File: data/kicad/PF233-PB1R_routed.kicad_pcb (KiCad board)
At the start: 4 copper layers, 70 x 70 mm, 39 parts, among them M12 12 V 1.5 A switching module, Q1A 650V SJ 95mR, Q1B 650V SJ 95mR, U1 TC4420, U3 LM393

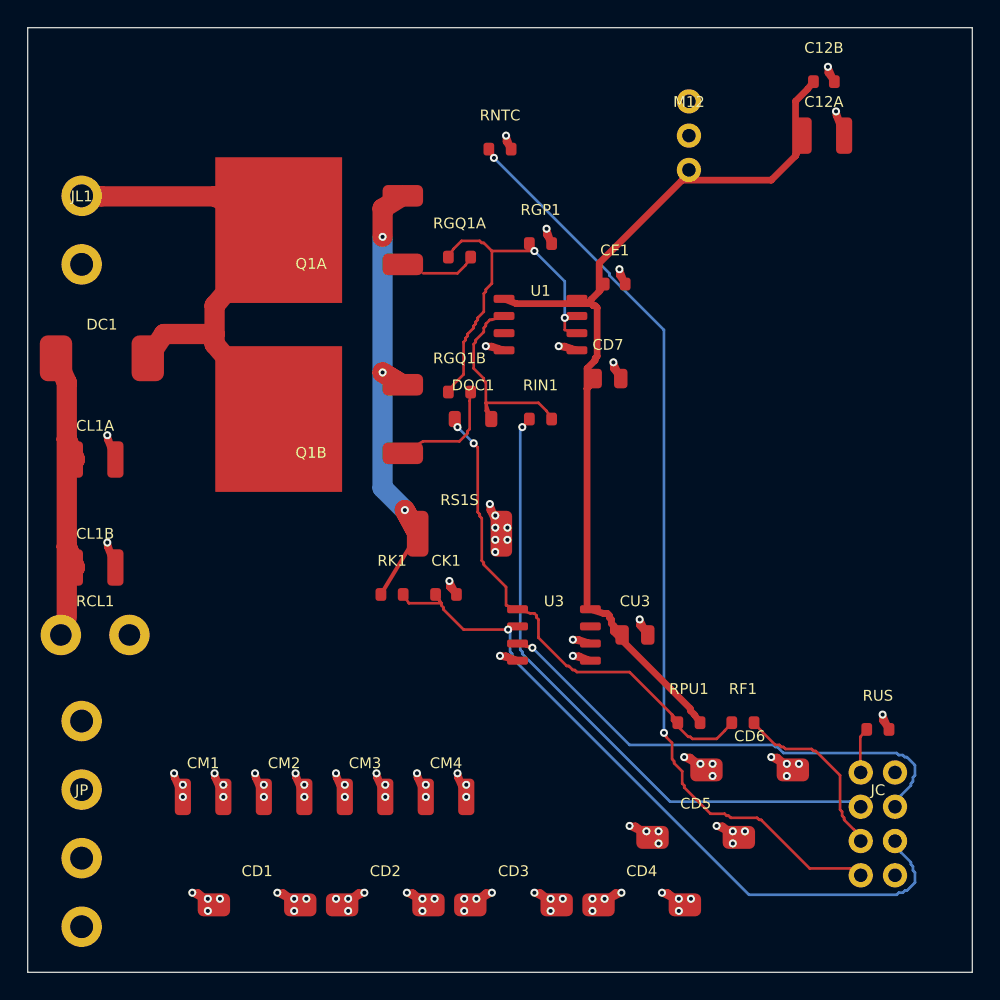
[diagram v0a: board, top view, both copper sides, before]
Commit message: Step 5: datasheets and fabricator sheets (vendor-derived floor, verified parts, PB1R 9-can bank, Gerber edge read-back)
- Fab floor from AdvancedPCB / TTM pages (docs/design/FAB_RULES_VERIFIED.md, U-FAB-RULES closed): clearance 0.16,
  component-PTH ring 0.18 / hole 0.46, drill-copper 0.26, drill-drill 0.41, every rule (severity error).
  CB1D JA/JB and HB2 TO-92 pads 1.02 mm; route_fix merges close same-net vias (CB1D, LB1).
- Parts from manufacturer PDFs (docs/design/DATASHEET_LOG.md): PB1R bulk 9 x Panasonic EEHZC1H101P
  (the 150 uF / 50 V polymer-Ta was not found; bank stays 900 uF, on-time table unchanged), PB1R re-placed
  with the Kelvin/comparator cluster pinned (pulse path 4.9 mohm, spike 7.5 V, ground ref 15.5 mV unchanged);
  SMCJ30A (SMCJ33A clamps 53.3 V > 50 V parts), Si4401FDY, BZT52C15, Bourns SF-1206S500-2 (new 1206 land),
  DRV5023BIQLPG, CRCW2512 500 V, OPA2365/OPA2211/LM393/CD74HC4051 checked. ES3J 600 V kept as a WATCH.
- U-DS-PARTS split into groups; open: TXDRIVE, OKI, PACK, BAV199, HVTERM. U-COLD-BOOTSTRAP closed.
- Controls retargeted to fixture folders (12/12). Netlist date fixed (data changed daily).
- Gerber planes from gerber_out.py ran into the notch and to 0.1 mm of the edge since r1 (found by the
  independent review): fixed, and gerber_edge_check.py reads every copper layer back.
- New Gerber sets CB1D_B3, LB1_v5, PB1R_v2; old sets marked SUPERSEDED.
- Findings for the owner: aluminium cans ~0.5 x a 1 g nugget (OPEN_ITEMS 34), OPA2365 capacitive load (30),
  OPA2211 input range on 5 V (31), Hall magnet spread (32).
- Strict regress 55 PASS / 0 FAIL / 0 SKIP; sign-off 44 PASS / 0 FAIL / 0 SKIP / 19 UNVERIFIED.

Co-Authored-By: Claude Opus 5.5 <noreply@anthropic.com>
Claude-Session: https://claude.ai/code/session_015VKhZtgEAWnezB2NDY75VV
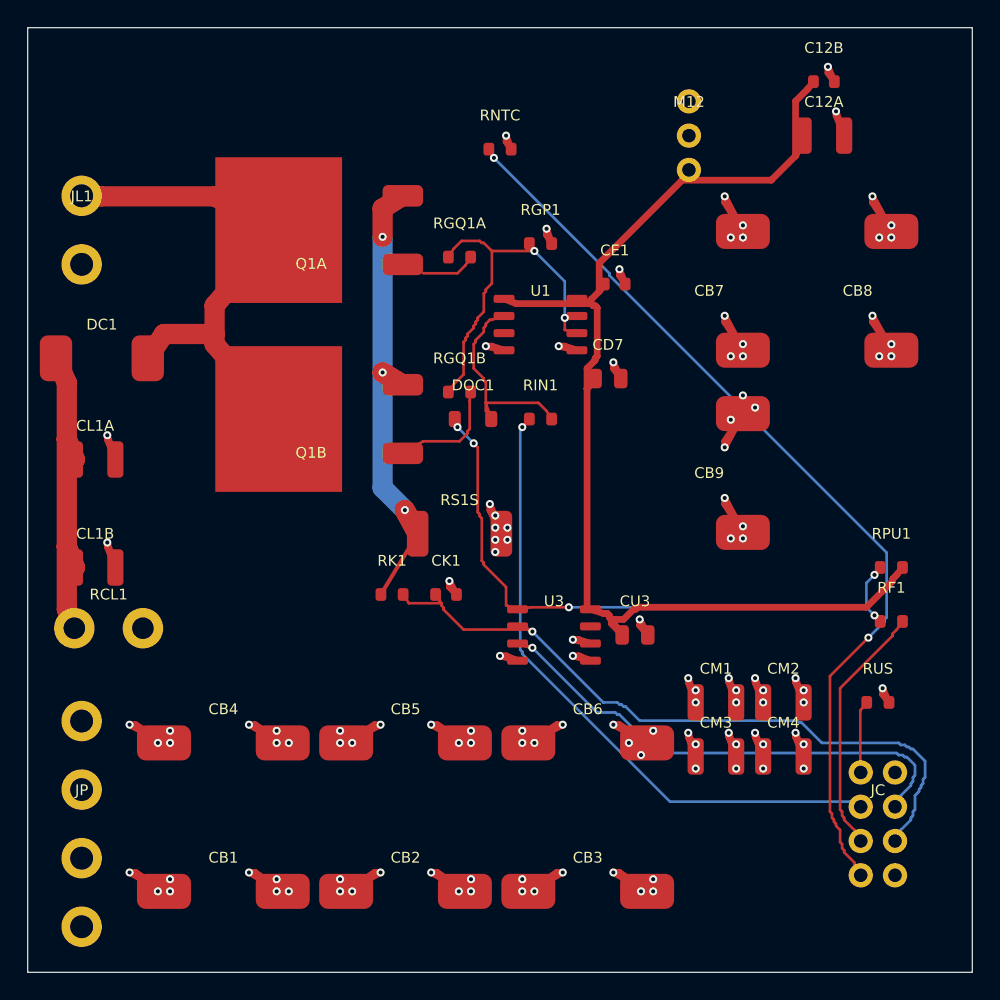
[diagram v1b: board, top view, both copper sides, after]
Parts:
- removed CD1, CD2, CD3, CD4, CD5, CD6: 150u 50V polymer Ta, Capacitor_Tantalum_SMD:CP_EIA-7343-43_Kemet-X
- added CB1: 100u 50V hybrid, Capacitor_SMD:CP_Elec_10x10, F.Cu at (79.5, 129.0)
- added CB2: 100u 50V hybrid, Capacitor_SMD:CP_Elec_10x10, F.Cu at (93.0, 129.0)
- added CB3: 100u 50V hybrid, Capacitor_SMD:CP_Elec_10x10, F.Cu at (106.5, 129.0)
- added CB4: 100u 50V hybrid, Capacitor_SMD:CP_Elec_10x10, F.Cu at (79.5, 118.0)
- added CB5: 100u 50V hybrid, Capacitor_SMD:CP_Elec_10x10, F.Cu at (93.0, 118.0)
- added CB6: 100u 50V hybrid, Capacitor_SMD:CP_Elec_10x10, F.Cu at (106.5, 118.0)
- added CB7: 100u 50V hybrid, Capacitor_SMD:CP_Elec_10x10, F.Cu at (118.0, 84.5)
- added CB8: 100u 50V hybrid, Capacitor_SMD:CP_Elec_10x10, F.Cu at (129.0, 84.5)
- added CB9: 100u 50V hybrid, Capacitor_SMD:CP_Elec_10x10, F.Cu at (118.0, 98.0)
- RS1S: value 10m 3W -> 10m 1W
- moved CM1 38.6 mm to (116.0, 115.0)
- moved CM2 37.7 mm to (121.0, 115.0)
- moved CM3 26.2 mm to (116.0, 119.0)
- moved CM4 25.2 mm to (121.0, 119.0)
- moved RPU1 18.9 mm to (129.0, 105.0)
- moved RF1 13.3 mm to (129.0, 109.0)
- moved RUS 2.00 mm to (128.0, 115.0)
- moved RCL1 1.12 mm to (71.0, 109.5)
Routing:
- net VBUS: track 45.7 -> 75.4 mm, vias 38 -> 50
- net GND: track 79.8 -> 109.0 mm, vias 57 -> 69
- net AUX12: track 82.0 -> 95.9 mm
- net OC1_OUT: track 38.5 -> 47.6 mm, vias 2 -> 5
- net FAULT1_N: track 13.4 -> 18.7 mm
- net UMB_SHLD: track 3.37 -> 5.36 mm
- net ISENSE1: track 54.0 -> 55.5 mm
- net CLAMP1: track 25.9 -> 26.8 mm

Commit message: WIP checkpoint (audit): PB1R/NPM fit fixed (NPM body v2 rails, dam v2, PB1R_v3), fit check and guards; source+data
Co-Authored-By: Claude Sonnet 5.5 <noreply@anthropic.com>
Claude-Session: https://claude.ai/code/session_015VKhZtgEAWnezB2NDY75VV
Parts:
- moved CB8 13.5 mm to (128.5, 98.0)
- moved CB6 13.0 mm to (118.0, 112.0)
- moved CB5 12.3 mm to (87.5, 107.0)
- moved CB3 11.2 mm to (104.5, 118.0)
- moved CB2 11.0 mm to (104.0, 129.0)
- moved RK1 6.50 mm to (98.5, 106.8)
- moved CM1 4.53 mm to (116.5, 119.5)
- moved CM2 4.53 mm to (121.5, 119.5)
- moved RS1S 4.50 mm to (101.5, 102.5)
- moved CM3 4.03 mm to (116.5, 123.0)
- moved CM4 4.03 mm to (121.5, 123.0)
- moved CK1 3.75 mm to (98.5, 109.8)
- moved DOC1 1.50 mm to (99.5, 94.0)
- moved RGQ1A 1.50 mm to (98.5, 82.0)
- moved RGQ1B 1.50 mm to (98.5, 92.0)
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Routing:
- net ISENSE1: track 55.5 -> 50.9 mm, vias 1 -> 2
- net DRVIN1: track 16.2 -> 12.2 mm
- net GATE_Q1A: track 4.11 -> 7.88 mm, vias 0 -> 2
- net TX1_IN: track 48.2 -> 45.1 mm, vias 1 -> 3
- net GATE_Q1B: track 8.41 -> 10.7 mm, vias 0 -> 2
- net G1: track 31.5 -> 29.7 mm
- net DRAIN1: track 38.6 -> 37.2 mm
- net SRC1: track 37.6 -> 36.3 mm, vias 3 -> 0
- net GND: track 109.0 -> 110.0 mm, vias 69 -> 66
- net AUX12: track 95.9 -> 95.1 mm
- net OC1_OUT: track 47.6 -> 47.2 mm, vias 5 -> 3
- net VBUS: vias 50 -> 49
